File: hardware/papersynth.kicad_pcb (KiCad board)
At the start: 2 copper layers, 200 x 48.5 mm, 106 parts, among them J1 USB_OTG, J2 JACK_2P, J3 Micro_SD_Card_Det, J4 JACK_TRS_5PINS, J5 JACK_2P, Q1 Q_NPN_BEC, Q2 Q_NPN_BEC, SW1 SW_Push, SW2 SW_Push, U1 CP2102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

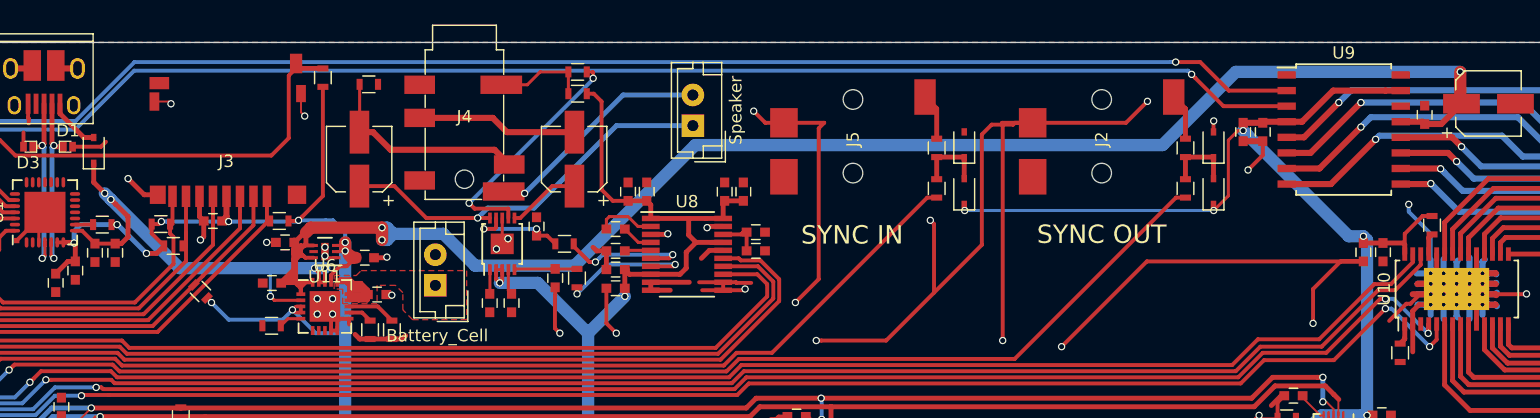
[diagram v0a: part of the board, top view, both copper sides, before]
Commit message: Swapped side of jacks
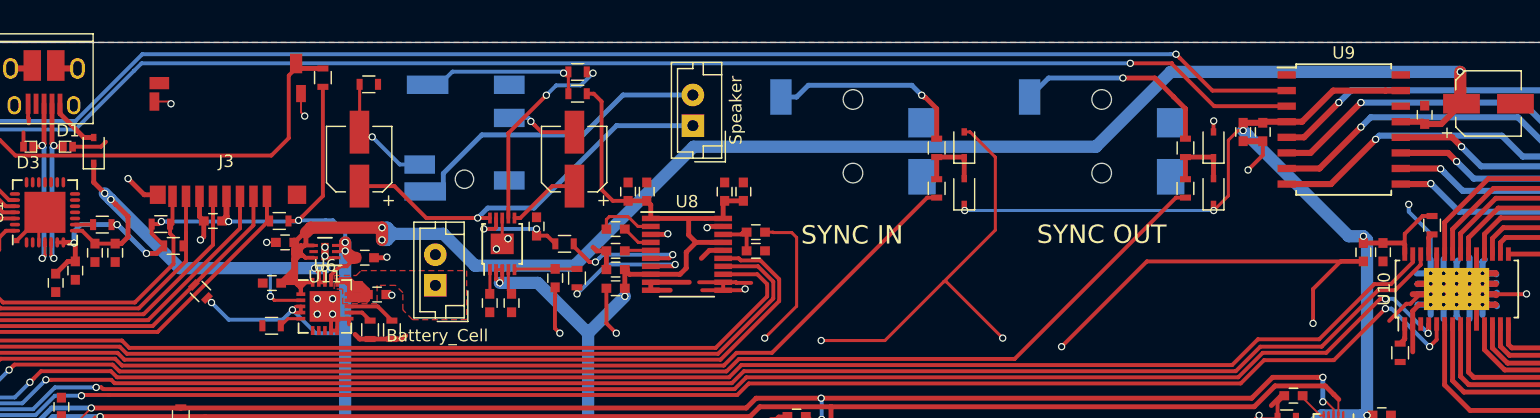
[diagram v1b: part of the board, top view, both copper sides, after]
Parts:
- J2, J4, J5: moved to B.Cu
- turned J4 to 180 degrees
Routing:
- net GND: track 291.1 -> 248.7 mm, vias 41 -> 38
- net Net-(J2-Pad1): track 3.79 -> 16.8 mm, vias 0 -> 1
- net Net-(J5-Pad1): track 3.79 -> 16.3 mm, vias 0 -> 1
- net Net-(C36-Pad2): track 17.2 -> 9.90 mm, vias 0 -> 1
- net Net-(C35-Pad2): track 13.1 -> 5.85 mm, vias 0 -> 1
- net Net-(J4-Pad5): track 18.8 -> 25.6 mm, vias 1 -> 0
- net Net-(J4-Pad4): track 7.68 -> 13.8 mm, vias 0 -> 1
- net Net-(R30-Pad2): track 19.5 -> 16.4 mm
- net /ESP32_MODULE/ROW_D: track 132.1 -> 132.7 mm
- net /ESP32_MODULE/ROW_C: track 130.6 -> 131.1 mm

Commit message: Stitched some planes
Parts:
- moved R23 13.5 mm to (164.3, 71.5)
- moved D4 13.5 mm to (166.6, 75.1)
- moved D5 13.5 mm to (166.6, 71.2)
- moved R24 13.5 mm to (164.3, 74.8)
- moved R25 13.3 mm to (144.2, 71.5)
- moved D6 13.3 mm to (146.5, 75.1)
- moved D7 13.3 mm to (146.5, 71.2)
- moved R26 13.3 mm to (144.2, 74.8)
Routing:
- net GND: track 248.7 -> 347.0 mm, vias 38 -> 42
- net Net-(J2-Pad1): track 16.8 -> 3.42 mm
- net Net-(J5-Pad1): track 16.3 -> 2.95 mm
- net /ESP32_MODULE/SYNC_OUT: track 125.2 -> 113.7 mm
- net +3V3: track 400.0 -> 396.6 mm, vias 22 -> 20
- net /ESP32_MODULE/SYNC_IN: track 103.3 -> 99.9 mm
